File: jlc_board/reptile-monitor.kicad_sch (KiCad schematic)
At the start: 25 parts, among them J1 AudioJack4_SwitchR1, J2 AudioJack4_SwitchR1, J3 PWR CONN, J5 UART, SW1 RESET, SW2 BOOT, U1 AP2112M-3.3, U2 TCA4307DGKR

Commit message: consolidate kicad libraries
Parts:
- added J5, J6: I2C, Connector_JST:JST_SH_SM04B-SRSS-TB_1x04-1MP_P1.00mm_Horizontal, symbol Connector:Conn_01x04_Male
- added R5, R6: 10k, Resistor_SMD:R_0603_1608Metric, symbol Device:R_Small
- D2: value BLUE -> BLU
- U1: footprint SamacSys_Parts:SOIC127P600X170-8N -> reptile-monitor:SOIC127P600X170-8N; symbol SamacSys_Parts:AP2112M-3.3TRG1 -> reptile-monitor:AP2112M-3.3TRG1
- renumbered J5 to J4
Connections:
- net +3V3: now also J5.3 (Pin_3), J6.3 (Pin_3), R5.1, R6.1
- net GND: now also J5.4 (Pin_4), J6.4 (Pin_4)
- net LED: now also MD1.30 (IO18); no longer MD1.4 (IO36)
- net SDA1: now reaches MD1.8 (IO32)
- net SDA1: now also RN1.3 (R2.2), U2.6 (SDAIN)
- net SCL1: now reaches MD1.9 (IO33)
- net SCL1: now also RN2.2 (R1.2), U2.3 (SCLIN)
- net IO4 renamed SCL0
- net SCL0: now also J5.1 (Pin_1), J6.1 (Pin_1), R6.2
- net IO5 renamed SDA0
- net SDA0: now also J5.2 (Pin_2), J6.2 (Pin_2), R5.2
- removed net SCL: MD1.12 (IO27), RN2.2 (R1.2), U2.3 (SCLIN)
- removed net SDA: MD1.13 (IO14), RN1.3 (R2.2), U2.6 (SDAIN)
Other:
- moved on the sheet: D2, R4

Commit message: rev4
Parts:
- added unit 4 of RN2
- RN1: LCSC Part (none) -> C110924
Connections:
- net SCL0: now also RN2.2 (R1.2), U2.3 (SCLIN)
- net SCL1: no longer RN2.2 (R1.2), U2.3 (SCLIN)
- net SCL_BUFFERED: no longer J2.2 (T)
- net SDA0: now also RN1.4 (R3.2), U2.6 (SDAIN)
- net SDA1: no longer RN1.3 (R2.2), U2.6 (SDAIN)
- net SDA_BUFFERED: now also RN1.3 (R2.2); no longer J2.3 (R1), RN1.4 (R3.2)
- net IO27: now reaches MD1.12 (IO27)
- net IO27: now also J2.3 (R1), RN2.5 (R4.2)
- no-connect marks 14 -> 13

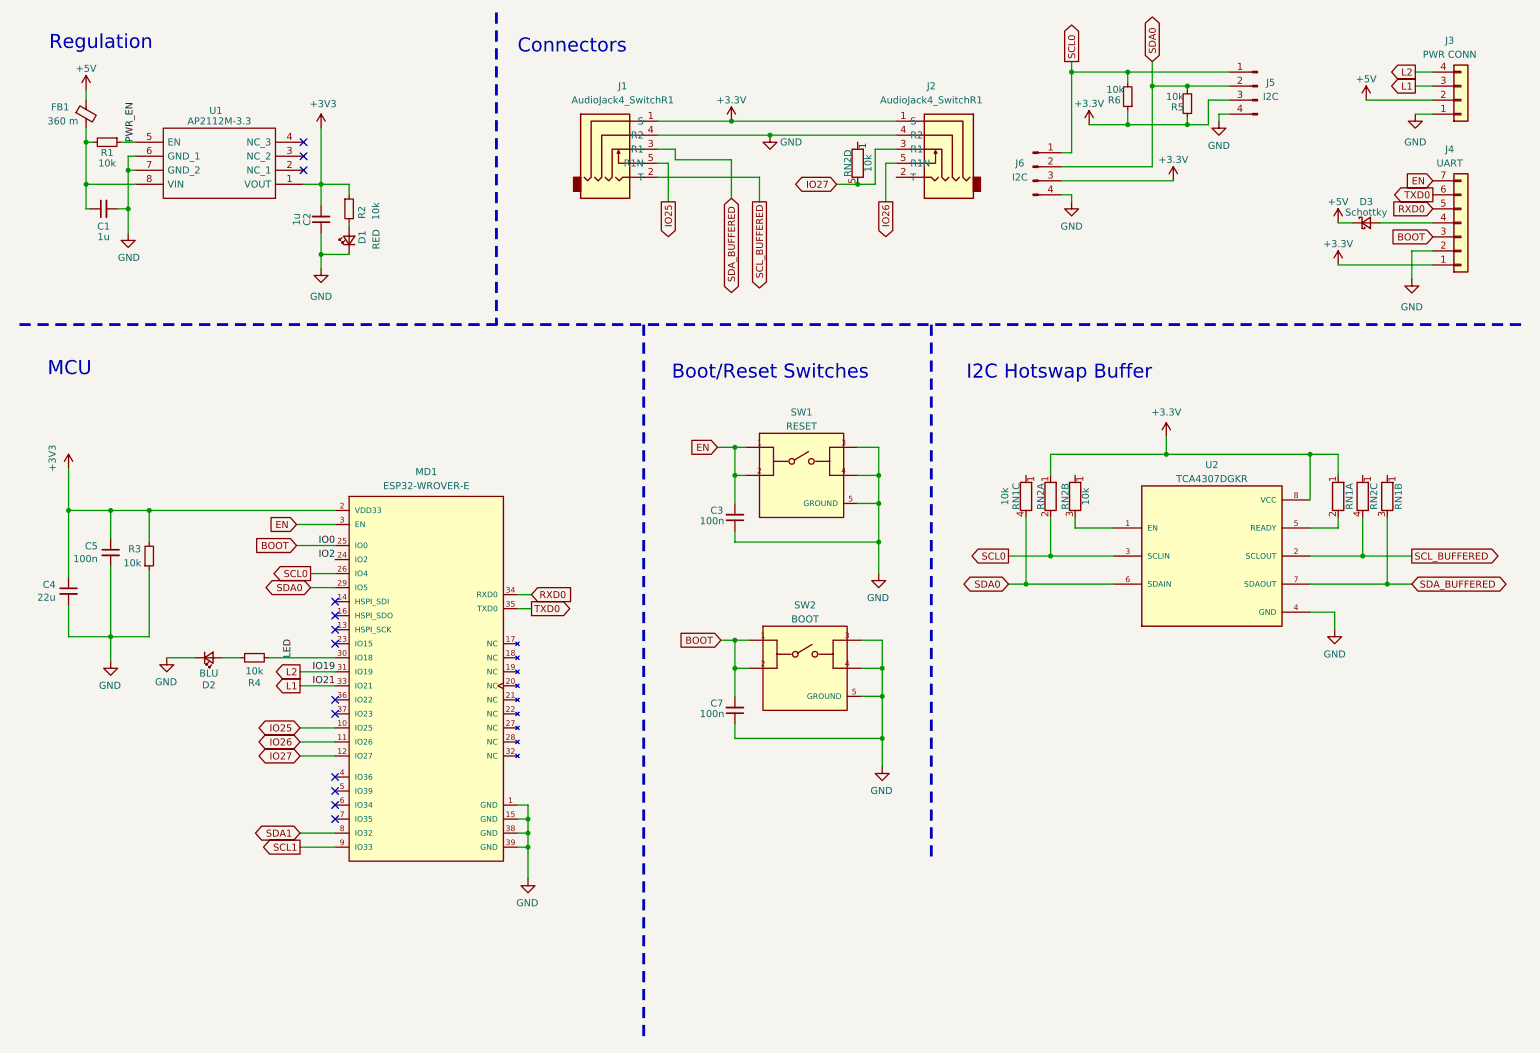
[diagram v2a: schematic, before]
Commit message: move quiic connector to same side as TRRS sensor connectors so that all connectors are on the same side
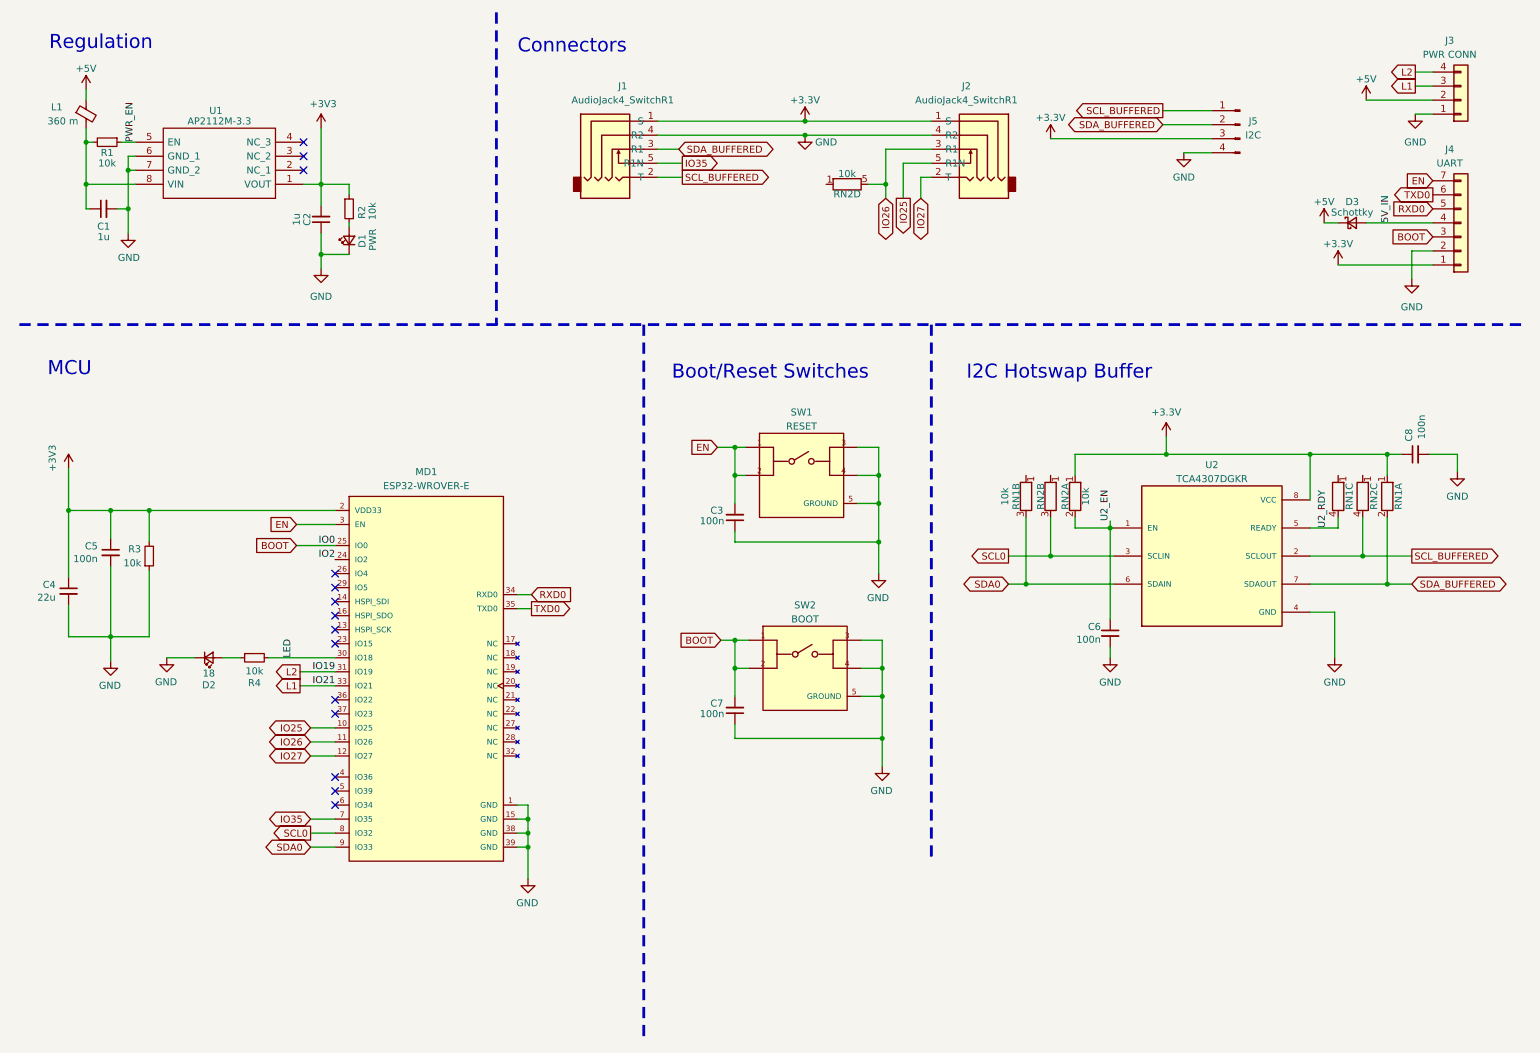
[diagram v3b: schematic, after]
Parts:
- removed J6: I2C, Connector_JST:JST_SH_SM04B-SRSS-TB_1x04-1MP_P1.00mm_Horizontal, symbol Connector:Conn_01x04_Male
- removed R5, R6: 10k, Resistor_SMD:R_0603_1608Metric, symbol Device:R_Small
- added C6, C8: 100n, reptile-monitor:C_0603_1608Metric, symbol Device:C_Small
- C1, C2, C3, C4, C5, C7: footprint Capacitor_SMD:C_0603_1608Metric -> reptile-monitor:C_0603_1608Metric
- D1: value RED -> PWR; footprint LED_SMD:LED_0603_1608Metric -> reptile-monitor:LED_0603_1608Metric
- D2: value BLU -> 18; footprint LED_SMD:LED_0603_1608Metric -> reptile-monitor:LED_0603_1608Metric
- D3: footprint Diode_SMD:D_SOD-523 -> reptile-monitor:D_SOD-523
- J3: footprint Connector_PinSocket_2.54mm:PinSocket_1x04_P2.54mm_Vertical -> reptile-monitor:PinSocket_1x04_P2.54mm_Vertical
- J4: footprint Connector_PinHeader_2.54mm:PinHeader_1x07_P2.54mm_Vertical -> reptile-monitor:PinHeader_1x07_P2.54mm_Vertical
- J5: footprint Connector_JST:JST_SH_SM04B-SRSS-TB_1x04-1MP_P1.00mm_Horizontal -> reptile-monitor:JST_SH_SM04B-SRSS-TB_1x04-1MP_P1.00mm_Horizontal
- L1: renamed from FB1; footprint Inductor_SMD:L_0603_1608Metric_Pad1.05x0.95mm_HandSolder -> reptile-monitor:L_0603_1608Metric
- R1, R2, R3, R4: footprint Resistor_SMD:R_0603_1608Metric -> reptile-monitor:R_0603_1608Metric
- RN1, RN2: footprint Resistor_SMD:R_Array_Convex_4x0603 -> reptile-monitor:R_Array_Convex_4x0603
- U2: footprint Package_SO:VSSOP-8_3.0x3.0mm_P0.65mm -> reptile-monitor:VSSOP-8_3.0x3.0mm_P0.65mm
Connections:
- net SCL1 is gone; now on net SDA0: MD1.9 (IO33)
- net SDA1 is gone; now on net SCL0: MD1.8 (IO32)
- net +3V3: now also RN1.1 (R1.1), RN2.1 (R1.1), C8.1; no longer RN1.1 (R1.1), RN2.1 (R1.1)
- net GND: now also C6.2, C8.2
- net IO25: now also J2.5 (R1N); no longer J1.5 (R1N)
- net IO26: now also J2.3 (R1), RN2.5 (R4.2); no longer J2.5 (R1N)
- net IO27: now also J2.2 (T); no longer J2.3 (R1), RN2.5 (R4.2)
- net SCL0: now also RN2.3 (R2.2); no longer J5.1 (Pin_1), MD1.26 (IO4), RN2.2 (R1.2)
- net SCL_BUFFERED: now also J5.1 (Pin_1)
- net SDA0: now also RN1.3 (R2.2); no longer J5.2 (Pin_2), MD1.29 (IO5), RN1.4 (R3.2)
- net SDA_BUFFERED: now also J5.2 (Pin_2), RN1.2 (R1.2); no longer RN1.3 (R2.2)
- net U2_EN: now reaches U2.1 (EN)
- net U2_EN: now also RN2.2 (R1.2), C6.1; no longer RN2.3 (R2.2)
- net U2_RDY: now reaches U2.5 (READY)
- net U2_RDY: now also RN1.4 (R3.2); no longer RN1.2 (R1.2)
- net 5V_IN: now reaches D3.2 (A), J4.4 (Pin_4)
- net IO35: now reaches MD1.7 (IO35)
- net IO35: now also J1.5 (R1N)
- no-connect marks 13 -> 14
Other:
- moved on the sheet: D3, J2, J5, RN1A, RN1C, RN2A, RN2B, RN2D

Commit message: v4 reorganization complete
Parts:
- removed C7: 100n, reptile-monitor:C_0603_1608Metric, symbol Device:C_Small
- removed SW2: BOOT, reptile-monitor:CK-KMR221GLFS-MFG, symbol Reptile_Monitor:KMR221GLFS
- added H1, H2: MountingHole, MountingHole:MountingHole_2.2mm_M2_ISO7380, symbol Mechanical:MountingHole
- added J6: 18-Lead FPC 0.5 mm - Vertical, reptile-monitor:TE_1-1734742-8, symbol reptile-monitor:18-Lead FPC 0.5 mm - Vertical
- D2: value 18 -> IO5
- D3: footprint reptile-monitor:D_SOD-523 -> reptile-monitor:D_SMA
- J3: footprint reptile-monitor:PinSocket_1x04_P2.54mm_Vertical -> reptile-monitor:PinSocket_1x04_P2.54mm_Vertical_SMD_Pin1Left
- J4: footprint reptile-monitor:PinHeader_1x07_P2.54mm_Vertical -> reptile-monitor:PinHeader_1x06_P2.54mm_Vertical; symbol Connector_Generic:Conn_01x07 -> Connector_Generic:Conn_01x06
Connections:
- net +3V3: now also J6.1; no longer J4.1 (Pin_1)
- net 5V_IN: now also J4.3 (Pin_3); no longer J4.4 (Pin_4)
- net BOOT: now also J4.2 (Pin_2); no longer J4.3 (Pin_3)
- net EN: now also J4.6 (Pin_6), R3.1, SW1.3, SW1.4; no longer J4.7 (Pin_7), SW1.1, SW1.2
- net GND: now also J4.1 (Pin_1), SW1.1, SW1.2, J6.3, J6.S1 (SHIELD), J6.S2 (SHIELD); no longer J4.2 (Pin_2), R3.1, SW1.3, SW1.4
- net IO25: now also J6.2; no longer J2.5 (R1N)
- net IO26: now also J6.7; no longer J2.3 (R1), RN2.5 (R4.2)
- net IO27: now also J6.8; no longer J2.2 (T)
- net L1: now also MD1.31 (IO19); no longer MD1.33 (IO21)
- net L2: now also MD1.30 (IO18); no longer MD1.31 (IO19)
- net LED: now also MD1.9 (IO33); no longer MD1.30 (IO18)
- net RXD0: now also J4.4 (Pin_4); no longer J4.5 (Pin_5)
- net SCL0: now also MD1.36 (IO22); no longer MD1.8 (IO32)
- net SDA0: now also MD1.33 (IO21); no longer MD1.9 (IO33)
- net TXD0: now also J4.5 (Pin_5); no longer J4.6 (Pin_6)
- net PWR_IN: now reaches C1.1, L1.2, R1.2, U1.8 (VIN)
- net SPI_SCK: now reaches MD1.13 (IO14)
- net SPI_SCK: now also J6.4
- net SPI_SDI: now reaches MD1.14 (IO12)
- net SPI_SDI: now also J6.5
- net SPI_SDO: now reaches MD1.16 (IO13)
- net SPI_SDO: now also J6.6
- net IO15: now reaches MD1.23 (IO15)
- net IO15: now also J1.5 (R1N)
- net IO4: now reaches MD1.26 (IO4)
- net IO4: now also J2.5 (R1N)
- net IO5: now reaches MD1.29 (IO5)
- net IO5: now also J2.3 (R1), RN2.5 (R4.2)
- net IO23: now reaches MD1.37 (IO23)
- net IO23: now also J2.2 (T)
- net IO35: no longer names the net of MD1.7 (IO35)
- net IO35: no longer J1.5 (R1N)
- new net IO28: J6.9
- no-connect marks 14 -> 16
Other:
- moved on the sheet: C1, C2, C3, C4, C5, C6, C8, D1, D2, D3, J1, J2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

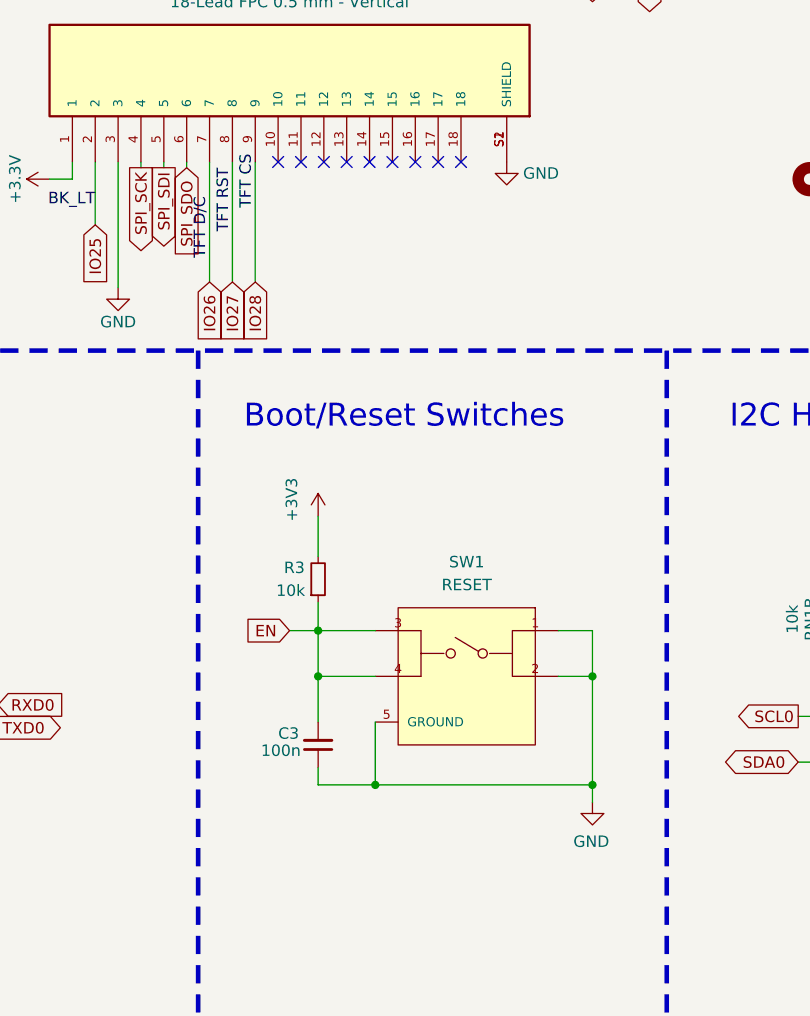
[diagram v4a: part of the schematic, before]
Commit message: add raight angle tactile switch
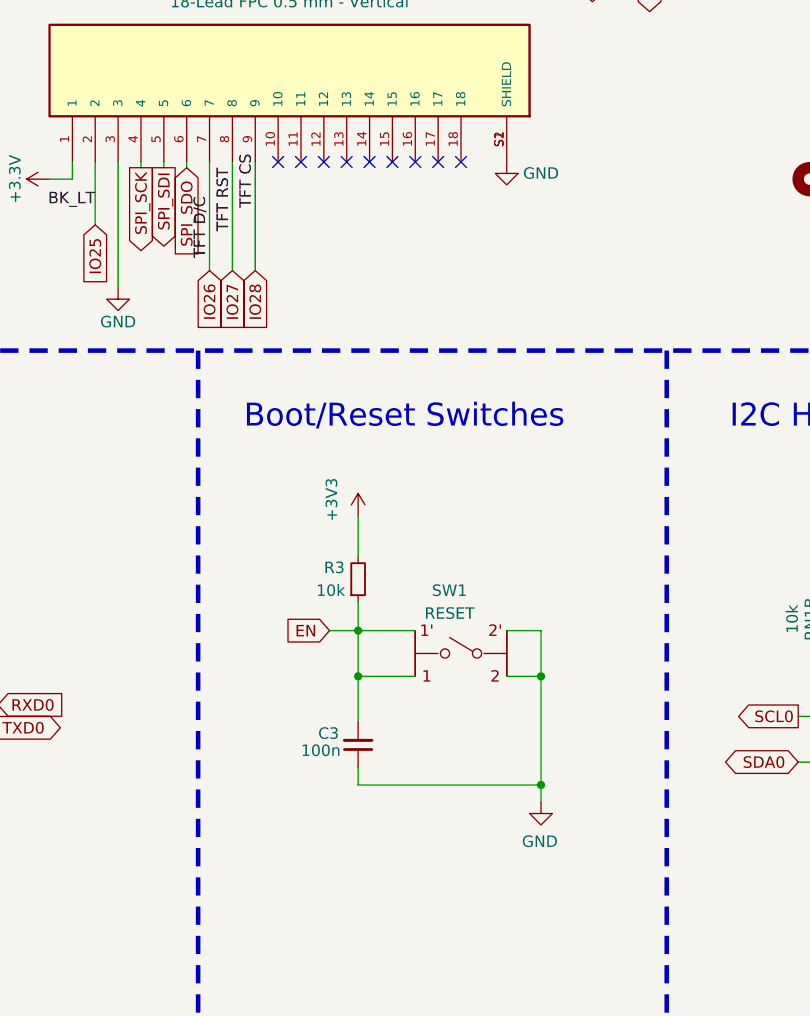
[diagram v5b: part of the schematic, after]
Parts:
- SW1: footprint reptile-monitor:CK-KMR221GLFS-MFG -> reptile-monitor:Panasonic-EVQ-P7A01P-0-0-MFG; symbol Reptile_Monitor:KMR221GLFS -> reptile-monitor:EVQ-P7A01P; contact resistance 100mΩ -> 500mΩ; digikey description SWITCH TACTILE SPST-NO 0.05A 32V -> SWITCH TACTILE SPST-NO 0.05A 12V; digikey part number 401-1427-1-ND -> P16763CT-ND; electromechanical life 200000Cycles -> 100000Cycles; height 1.9mm -> 1.55mm; library id ae41f1c5fc8639fe -> 2f293019bba4f771; manufacturer C&K -> Panasonic; mouser description Tactile Switches SPST Rnd Bttn Gull .05A 32VDC 1W SMDr\n -> SWITCH TACTILE SPST-NO 0.05A 12V; mouser part number 611-KMR221G-LFS -> 667-EVQP7A01P; operating force 2N -> 2.2N; package SMT5_TACT_SWITCH -> SMT_SW_3MM5_2MM9; temperature range high +85°C -> +70°C; temperature range low -40°C -> -20°C; voltage rating DC 32V -> 12V
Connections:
- net EN: now also SW1.1, SW1.1'; no longer SW1.3, SW1.4
- net GND: now also SW1.2'; no longer SW1.1, SW1.5 (GROUND)
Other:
- moved on the sheet: C3, R3

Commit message: updates
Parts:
- added D4: BAS316, reptile-monitor:D_SOD-323, symbol Diode:BAS316
- added LS1: AST7525MATRQ, reptile-monitor:Mallory_Sonalert_Products_Inc-AST7525MATRQ-0-0-MFG, symbol reptile-monitor:AST7525MATRQ
- added Q1: 2SC1741, Package_TO_SOT_SMD:SOT-23, symbol Transistor_BJT:2SC1815
- added R5: 1k, reptile-monitor:R_0603_1608Metric, symbol Device:R_Small
- D3: footprint reptile-monitor:D_SMA -> reptile-monitor:D_SOD-323
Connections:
- net GND: now also Q1.1 (E)
- net LED: now also MD1.8 (IO32); no longer MD1.9 (IO33)
- new net: D4.2 (A), LS1.4 (CATHODE), Q1.2 (C)
- new net: Q1.3 (B), R5.2
- new net: D4.1 (K), LS1.3 (ANODE)
- new net SPK: MD1.9 (IO33), R5.1
- no-connect marks 16 -> 18
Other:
- title: (none) -> Reptile Monitor
- moved on the sheet: C3, D2, R3, R4, SW1

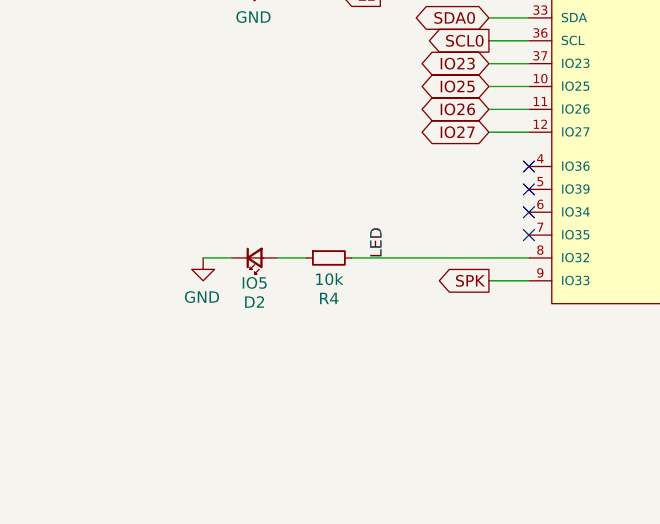
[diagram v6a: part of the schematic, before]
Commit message: Change LED value to remove IO5 confusion
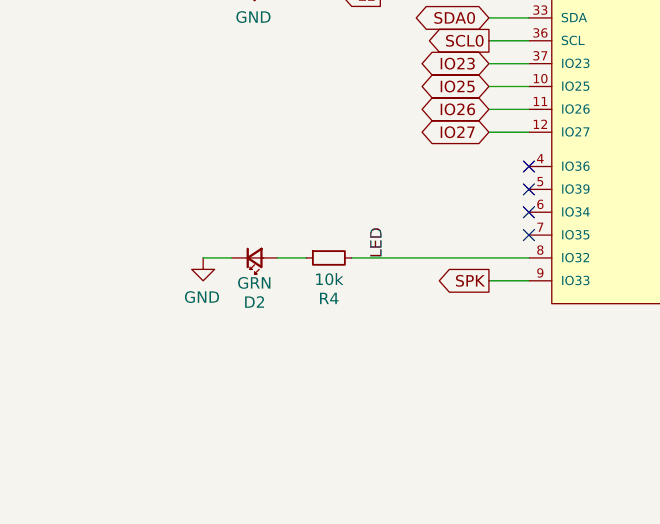
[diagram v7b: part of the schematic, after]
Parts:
- D2: value IO5 -> GRN
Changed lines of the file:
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@@
     (in_bom yes) (on_board yes)
     (property "Reference" "D2" (id 0) (at 36.83 175.133 0))
-    (property "Value" "IO5" (id 1) (at 36.83 172.9994 0))
+    (property "Value" "GRN" (id 1) (at 36.83 172.9994 0))
     (property "Footprint" "reptile-monitor:LED_0603_1608Metric" (id 2) (at 36.83 170.18 90)
       (effects (font (size 1.27 1.27)) hide)
@@
     )
     (path "/fc079a75-5d2a-4a20-adc7-e530c9b8fd5b"
-      (reference "D2") (unit 1) (value "IO5") (footprint "reptile-monitor:LED_0603_1608Metric")
+      (reference "D2") (unit 1) (value "GRN") (footprint "reptile-monitor:LED_0603_1608Metric")
     )
     (path "/7556ce11-7b17-4f6a-aeac-b8d0b54b9356"

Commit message: rev4.5
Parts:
- removed D3: Schottky, reptile-monitor:D_SOD-323, symbol Device:D_Schottky_Small
- removed J5: I2C, reptile-monitor:JST_SH_SM04B-SRSS-TB_1x04-1MP_P1.00mm_Horizontal, symbol Connector:Conn_01x04_Male
- added TP1: TestPoint_2Pole, Connector_PinHeader_2.54mm:PinHeader_1x02_P2.54mm_Vertical, symbol Connector:TestPoint_2Pole
- D2: value GRN -> 32
- RN1, RN2: footprint reptile-monitor:R_Array_Convex_4x0603 -> reptile-monitor:Panasonic-EXB-V8V103JV-0; symbol Device:R_Network04_Split -> reptile-monitor:EXB-V8V103JV; category (none) -> Res; digikey description (none) -> RES ARRAY 4 RES 10K OHM 1206; digikey part number (none) -> Y4103CT-ND; lead free (none) -> yes; library id (none) -> 88bf4eae5d762cba; manufacturer (none) -> Panasonic; mouser part number (none) -> 667-EXB-V8V103JV; package (none) -> 1206 (3216 metric); resistance (none) -> 10kΩ; rohs (none) -> yes; temperature range high (none) -> +125°C; temperature range low (none) -> -55°C
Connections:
- net 5V_IN is gone; now on net +5V: J4.3 (Pin_3)
- net +3V3: now also RN1.2, RN1.3, RN2.2, RN2.3, RN2.4, U1.2 (NC_1), U1.3 (NC_2)
- net GND: now also TP1.1
- net IO5: now also RN2.6; no longer RN2.5 (R4.2)
- net PWR_IN: now also TP1.2
- net SCL0: now also RN2.7; no longer RN2.3 (R2.2)
- net SCL_BUFFERED: now also RN2.5; no longer RN2.4 (R3.2)
- net SDA0: now also RN1.7; no longer RN1.3 (R2.2)
- net SDA_BUFFERED: now also RN1.8; no longer RN1.2 (R1.2)
- net U2_EN: now also RN2.8; no longer RN2.2 (R1.2)
- net U2_RDY: now also RN1.6; no longer RN1.4 (R3.2)
- net LED renamed IO32
- no-connect marks 18 -> 16
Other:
- moved on the sheet: C8, D2, H1, H2, J1, J2, J6, R4
